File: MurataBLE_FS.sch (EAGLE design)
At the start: 48 parts, among them CON2 C-2395.microSD, IC1 74LVC1G00DBV, IC2 IC_DCDC_LM27313, IC3 IC_LPC11U3XQFN33, IC4 IC_LDO_XX1117_4, IC5 1265-1139-1-ND, Q1 CLOCK_CRYSTAL_4_3225, SW1 SW_TACTSW_2PP8073, SW2 SW_TACTSW_2PP8073, SW3 SW_TACTSW_2PP8073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

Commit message: [ FS ] add LED1/R13/R14
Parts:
- added LED1: (no value), mylib:LED_1SEG_A2K1
- added R13, R14: 100/1005, mylib:R_US_PAD_PAD_1005
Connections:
- new net N$14: LED1.A1, R14.2
- new net N$3: IC3.P0_4/SCL, R13.1
- new net N$6: IC3.P0_5/SDA, R14.1
- new net N$9: LED1.A2, R13.2
- net GND: now also LED1.K1
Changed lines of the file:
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@@
 <part name="C16" library="mylib" deviceset="C_PAD_PAD_" device="1005" value="0.1u"/>
 <part name="SUPPLY4" library="mylib" deviceset="GND" device=""/>
+<part name="R13" library="mylib" deviceset="R_US_PAD_PAD" device="_1005" value="100/1005"/>
+<part name="R14" library="mylib" deviceset="R_US_PAD_PAD" device="_1005" value="100/1005"/>
+<part name="LED1" library="mylib" deviceset="LED_1SEG_A2K1" device=""/>
+<part name="SUPPLY5" library="mylib" deviceset="GND" device=""/>
 </parts>
 <sheets>
@@
 <instance part="C16" gate="G$1" x="198.12" y="-78.74" rot="R90"/>
 <instance part="SUPPLY4" gate="GND" x="205.74" y="-81.28"/>
+<instance part="R13" gate="G$1" x="167.64" y="139.7"/>
+<instance part="R14" gate="G$1" x="167.64" y="137.16"/>
+<instance part="LED1" gate="G$1" x="187.96" y="132.08"/>
+<instance part="SUPPLY5" gate="GND" x="187.96" y="124.46"/>
 </instances>
 <busses>
@@
 <pinref part="SUPPLY4" gate="GND" pin="GND"/>
 <wire x1="200.66" y1="-78.74" x2="205.74" y2="-78.74" width="0.1524" layer="91"/>
+</segment>
+<segment>
+<pinref part="LED1" gate="G$1" pin="K1"/>
+<pinref part="SUPPLY5" gate="GND" pin="GND"/>
 </segment>
 </net>
@@
 </segment>
 </net>
+<net name="N$3" class="0">
+<segment>
+<pinref part="IC3" gate="G$1" pin="P0_4/SCL"/>
+<pinref part="R13" gate="G$1" pin="1"/>
+<wire x1="160.02" y1="139.7" x2="165.1" y2="139.7" width="0.1524" layer="91"/>
+</segment>
+</net>
+<net name="N$6" class="0">
+<segment>
+<pinref part="R14" gate="G$1" pin="1"/>
+<pinref part="IC3" gate="G$1" pin="P0_5/SDA"/>
+<wire x1="165.1" y1="137.16" x2="160.02" y2="137.16" width="0.1524" layer="91"/>
+</segment>
+</net>
+<net name="N$9" class="0">
+<segment>
+<pinref part="R13" gate="G$1" pin="2"/>
+<pinref part="LED1" gate="G$1" pin="A2"/>
+<wire x1="170.18" y1="139.7" x2="190.5" y2="139.7" width="0.1524" layer="91"/>
+<wire x1="190.5" y1="139.7" x2="190.5" y2="134.62" width="0.1524" layer="91"/>
+</segment>
+</net>
+<net name="N$14" class="0">
+<segment>
+<pinref part="R14" gate="G$1" pin="2"/>
+<pinref part="LED1" gate="G$1" pin="A1"/>
+<wire x1="170.18" y1="137.16" x2="185.42" y2="137.16" width="0.1524" layer="91"/>
+<wire x1="185.42" y1="137.16" x2="185.42" y2="134.62" width="0.1524" layer="91"/>
+</segment>
+</net>

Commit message: [ FS ] silk move
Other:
- note added: "->RX"
- note added: "<-TX"
- moved on the sheet: R5, R6
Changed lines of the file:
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@@
 <plain>
 <text x="162.56" y="5.08" size="12.7" layer="94">r0.1</text>
+<text x="198.12" y="93.98" size="1.778" layer="94">-&gt;RX</text>
+<text x="198.12" y="96.52" size="1.778" layer="94">&lt;-TX</text>
 </plain>
 <instances>
@@
 <instance part="TP2" gate="G$1" x="124.46" y="15.24" rot="R270"/>
 <instance part="IC3" gate="G$1" x="137.16" y="154.94"/>
-<instance part="C8" gate="G$1" x="35.56" y="63.5"/>
+<instance part="C8" gate="G$1" x="35.56" y="63.5" rot="MR0"/>
 <instance part="C9" gate="G$1" x="58.42" y="63.5"/>
 <instance part="SUPPLY12" gate="GND" x="45.72" y="50.8"/>
@@
 <instance part="C10" gate="G$1" x="106.68" y="119.38"/>
 <instance part="C11" gate="G$1" x="99.06" y="119.38"/>
-<instance part="R5" gate="G$1" x="185.42" y="93.98"/>
-<instance part="R6" gate="G$1" x="185.42" y="96.52"/>
+<instance part="R5" gate="G$1" x="187.96" y="93.98"/>
+<instance part="R6" gate="G$1" x="187.96" y="96.52"/>
 <instance part="R7" gate="G$1" x="101.6" y="149.86"/>
 <instance part="R8" gate="G$1" x="101.6" y="144.78"/>
@@
 <segment>
 <pinref part="R6" gate="G$1" pin="2"/>
-<wire x1="187.96" y1="96.52" x2="190.5" y2="96.52" width="0.1524" layer="91"/>
+<wire x1="190.5" y1="96.52" x2="198.12" y2="96.52" width="0.1524" layer="91"/>
 </segment>
 <segment>
@@
 <segment>
 <pinref part="R5" gate="G$1" pin="2"/>
-<wire x1="187.96" y1="93.98" x2="190.5" y2="93.98" width="0.1524" layer="91"/>
+<wire x1="190.5" y1="93.98" x2="198.12" y2="93.98" width="0.1524" layer="91"/>
 </segment>
 <segment>
@@
 <pinref part="R6" gate="G$1" pin="1"/>
 <pinref part="IC3" gate="G$1" pin="P0_18/RXD&lt;-"/>
-<wire x1="160.02" y1="96.52" x2="182.88" y2="96.52" width="0.1524" layer="91"/>
+<wire x1="160.02" y1="96.52" x2="185.42" y2="96.52" width="0.1524" layer="91"/>
 <label x="165.1" y="96.52" size="1.778" layer="95"/>
 </segment>
@@
 <pinref part="IC3" gate="G$1" pin="P0_19/TXD-&gt;"/>
 <pinref part="R5" gate="G$1" pin="1"/>
-<wire x1="182.88" y1="93.98" x2="160.02" y2="93.98" width="0.1524" layer="91"/>
+<wire x1="185.42" y1="93.98" x2="160.02" y2="93.98" width="0.1524" layer="91"/>
 <label x="165.1" y="93.98" size="1.778" layer="95"/>
 </segment>

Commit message: [ FIX ] library update
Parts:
- IC5: value 1265-1139-1-ND -> IC_MEMORY_8P__TSSOP; device mylib:IC_SRAM_23K256_256K_32KBST -> mylib:IC_MEMORY_8P_AT25XE011_TSSOP
- Q1: value CLOCK_CRYSTAL_4_3225 -> (none)
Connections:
- net 3.3V renamed VCC
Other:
- moved on the sheet: C16, C2

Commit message: [ FS ] TP1/2; library update
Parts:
- IC5: value IC_MEMORY_8P__TSSOP -> IC_MEMORY_8P_AT25XE011_TSSOP
- PCB1: device dp_pcb:PCB_DP_RECTANGLE-43X70 -> dp_pcb_local:PCB_DP_RECTANGLE-43X70
- TP1: value TPPAD1-13 -> P7592
- TP2: value TPPAD1-13 -> P7591
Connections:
- net BL: now also IC3.BL/P1_19; no longer IC3.BL
- net ISP: now also IC3.ISP/P0_1; no longer IC3.ISP
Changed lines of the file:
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@@
 <parts>
 <part name="FRAME1" library="frames" deviceset="A4L-LOC" device=""/>
-<part name="PCB1" library="dp_pcb" deviceset="PCB_DP_RECTANGLE" device="-43X70" value="PCB_DP_RECTANGLE-43X70"/>
+<part name="PCB1" library="dp_pcb_local" deviceset="PCB_DP_RECTANGLE" device="-43X70" value="PCB_DP_RECTANGLE-43X70"/>
 <part name="IC1" library="74xx-little-us_local" deviceset="74*1G00" device="DBV" technology="LVC"/>
 <part name="CON1" library="mylib" deviceset="CON_USB" device="UB"/>
@@
 <part name="X1" library="con-samtec.local" deviceset="TSW-102-02-S-S" device=""/>
 <part name="C7" library="mylib" deviceset="C_PAD_PAD_" device="1608" value="0.1u"/>
-<part name="TP1" library="testpad_local" deviceset="TP" device="PAD1-13"/>
-<part name="TP2" library="testpad_local" deviceset="TP" device="PAD1-13"/>
+<part name="TP1" library="testpad_local" deviceset="TP" device="PAD1-13" value="P7592"/>
+<part name="TP2" library="testpad_local" deviceset="TP" device="PAD1-13" value="P7591"/>
 <part name="IC3" library="mylib" deviceset="IC_LPC11U3XQFN33" device=""/>
 <part name="C8" library="mylib" deviceset="C_PAD_PAD_" device="2125" value="4.7u/1608"/>
@@
 <part name="FRAME2" library="frames" deviceset="A4L-LOC" device=""/>
 <part name="SUPPLY24" library="mylib" deviceset="GND" device=""/>
-<part name="IC5" library="mylib" deviceset="IC_MEMORY_8P_*" device="_TSSOP" technology="AT25XE011" value="IC_MEMORY_8P__TSSOP"/>
+<part name="IC5" library="mylib" deviceset="IC_MEMORY_8P_*" device="_TSSOP" technology="AT25XE011" value="IC_MEMORY_8P_AT25XE011_TSSOP"/>
 <part name="SUPPLY25" library="mylib" deviceset="GND" device=""/>
 <part name="C16" library="mylib" deviceset="C_PAD_PAD_" device="1005" value="0.1u"/>
@@
 <segment>
 <pinref part="R9" gate="G$1" pin="2"/>
-<pinref part="IC3" gate="G$1" pin="ISP"/>
+<pinref part="IC3" gate="G$1" pin="ISP/P0_1"/>
 <wire x1="104.14" y1="142.24" x2="114.3" y2="142.24" width="0.1524" layer="91"/>
 <label x="116.84" y="142.24" size="1.778" layer="95" rot="R180"/>
@@
 <net name="BL" class="0">
 <segment>
-<pinref part="IC3" gate="G$1" pin="BL"/>
+<pinref part="IC3" gate="G$1" pin="BL/P1_19"/>
 <pinref part="R8" gate="G$1" pin="2"/>
 <wire x1="114.3" y1="144.78" x2="104.14" y2="144.78" width="0.1524" layer="91"/>

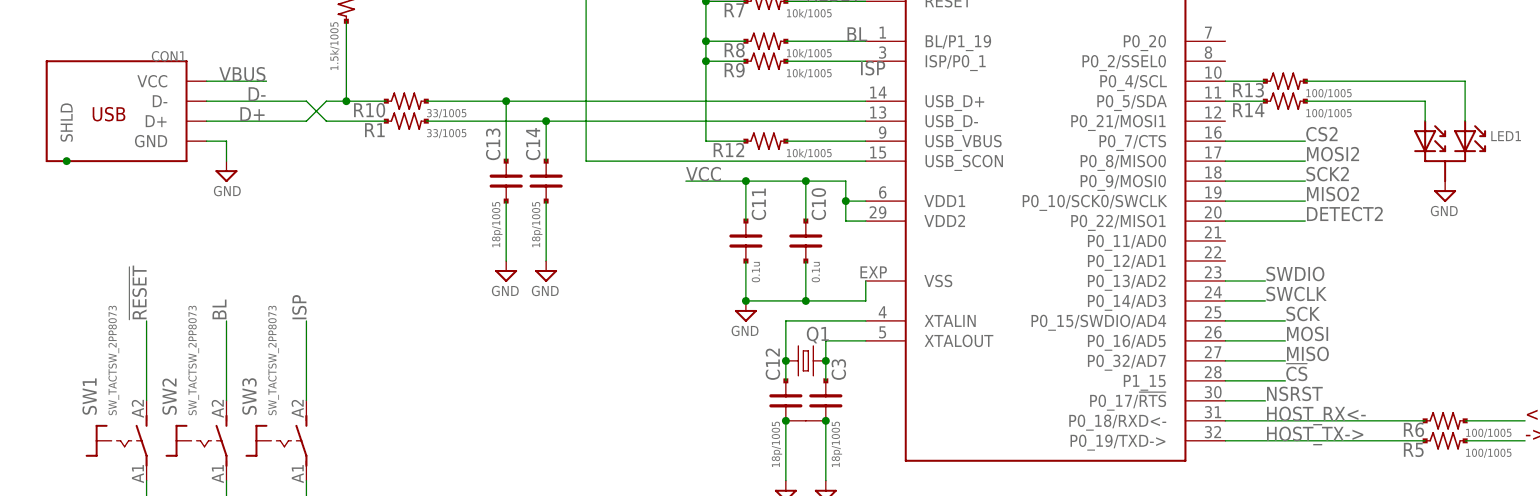
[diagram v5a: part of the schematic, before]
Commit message: [ FS ] library update CON2/4; pin connection shift to avoid SWD pins
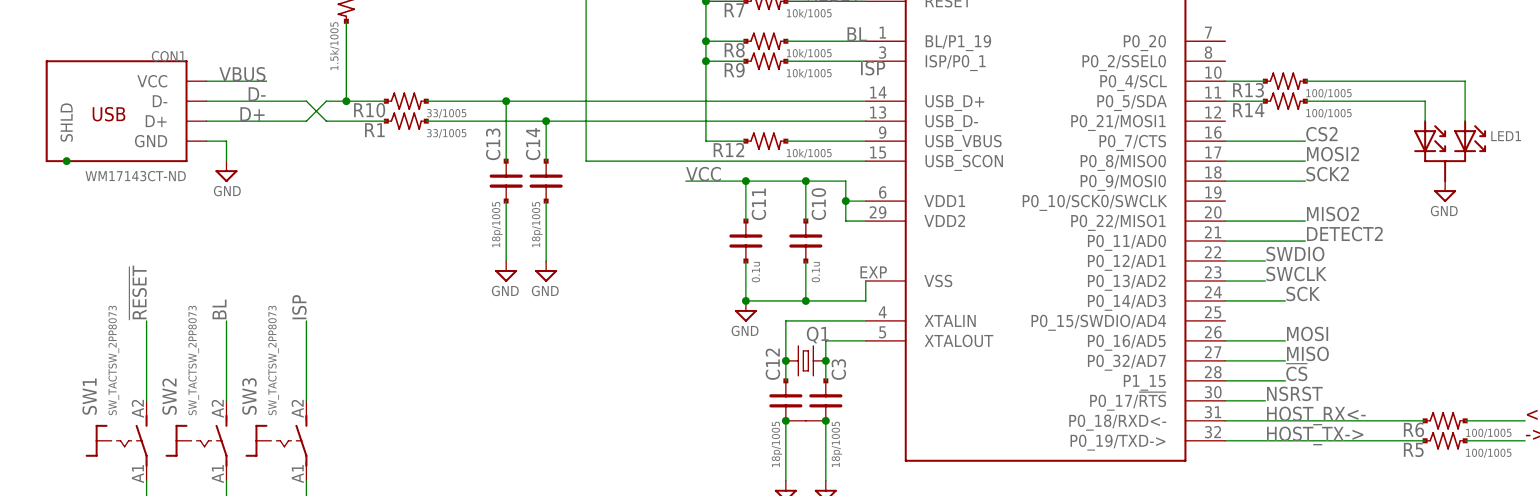
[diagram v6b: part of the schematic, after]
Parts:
- CON1: value (none) -> WM17143CT-ND; device mylib:CON_USBUB -> mylib:CON_USBMICROBUB
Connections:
- net DETECT2: now also IC3.P0_11/AD0; no longer IC3.P0_22/MISO1
- net MISO2: now also IC3.P0_22/MISO1; no longer IC3.P0_10/SCK0/SWCLK
- net SCK: now also IC3.P0_14/AD3; no longer IC3.P0_15/SWDIO/AD4
- net SWCLK: now also IC3.P0_13/AD2; no longer IC3.P0_14/AD3
- net SWDIO: now also IC3.P0_12/AD1; no longer IC3.P0_13/AD2
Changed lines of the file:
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@@
 <part name="PCB1" library="dp_pcb_local" deviceset="PCB_DP_RECTANGLE" device="-43X70" value="PCB_DP_RECTANGLE-43X70"/>
 <part name="IC1" library="74xx-little-us_local" deviceset="74*1G00" device="DBV" technology="LVC"/>
-<part name="CON1" library="mylib" deviceset="CON_USB" device="UB"/>
+<part name="CON1" library="mylib" deviceset="CON_USB" device="UB" technology="MICROB" value="WM17143CT-ND"/>
 <part name="SUPPLY1" library="mylib" deviceset="GND" device=""/>
 <part name="SUPPLY3" library="mylib" deviceset="GND" device=""/>
@@
 </segment>
 <segment>
-<wire x1="160.02" y1="111.76" x2="165.1" y2="111.76" width="0.1524" layer="91"/>
-<pinref part="IC3" gate="G$1" pin="P0_14/AD3"/>
-<label x="165.1" y="111.76" size="1.778" layer="95"/>
+<wire x1="160.02" y1="114.3" x2="165.1" y2="114.3" width="0.1524" layer="91"/>
+<pinref part="IC3" gate="G$1" pin="P0_13/AD2"/>
+<label x="165.1" y="114.3" size="1.778" layer="95"/>
 </segment>
 </net>
@@
 </segment>
 <segment>
-<wire x1="160.02" y1="114.3" x2="165.1" y2="114.3" width="0.1524" layer="91"/>
-<pinref part="IC3" gate="G$1" pin="P0_13/AD2"/>
-<label x="165.1" y="114.3" size="1.778" layer="95"/>
+<wire x1="160.02" y1="116.84" x2="165.1" y2="116.84" width="0.1524" layer="91"/>
+<pinref part="IC3" gate="G$1" pin="P0_12/AD1"/>
+<label x="165.1" y="116.84" size="1.778" layer="95"/>
 </segment>
 </net>
@@
 </segment>
 <segment>
-<wire x1="167.64" y1="109.22" x2="160.02" y2="109.22" width="0.1524" layer="91"/>
-<pinref part="IC3" gate="G$1" pin="P0_15/SWDIO/AD4"/>
-<label x="167.64" y="109.22" size="1.778" layer="95"/>
+<wire x1="167.64" y1="111.76" x2="160.02" y2="111.76" width="0.1524" layer="91"/>
+<pinref part="IC3" gate="G$1" pin="P0_14/AD3"/>
+<label x="167.64" y="111.76" size="1.778" layer="95"/>
 </segment>
 </net>
@@
 </segment>
 <segment>
-<wire x1="160.02" y1="124.46" x2="170.18" y2="124.46" width="0.1524" layer="91"/>
-<pinref part="IC3" gate="G$1" pin="P0_10/SCK0/SWCLK"/>
-<label x="170.18" y="124.46" size="1.778" layer="95"/>
+<wire x1="160.02" y1="121.92" x2="170.18" y2="121.92" width="0.1524" layer="91"/>
+<pinref part="IC3" gate="G$1" pin="P0_22/MISO1"/>
+<label x="170.18" y="121.92" size="1.778" layer="95"/>
 </segment>
 </net>
@@
 <net name="DETECT2" class="0">
 <segment>
-<pinref part="IC3" gate="G$1" pin="P0_22/MISO1"/>
-<wire x1="160.02" y1="121.92" x2="170.18" y2="121.92" width="0.1524" layer="91"/>
-<label x="170.18" y="121.92" size="1.778" layer="95"/>
-</segment>
-<segment>
 <wire x1="223.52" y1="154.94" x2="233.68" y2="154.94" width="0.1524" layer="91"/>
 <pinref part="CON2" gate="G$1" pin="SW_B"/>
 <label x="223.52" y="154.94" size="1.778" layer="95" rot="MR0"/>
 </segment>
-</net>
+<segment>
+<wire x1="160.02" y1="119.38" x2="170.18" y2="119.38" width="0.1524" layer="91"/>
+<pinref part="IC3" gate="G$1" pin="P0_11/AD0"/>
+<label x="170.18" y="119.38" size="1.778" layer="95"/>
+</segment>
+</net>
